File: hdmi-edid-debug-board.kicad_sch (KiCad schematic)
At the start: 87 parts, among them J1 HDMI-A_WE_685119134923, J4 HDMI-A_WE_685119134923, J5 USB-C_GCT_USB4105-GF-A, J6 JST_SH_1x4_SM04B-SRSS-TB-LF-SN, J7 PinHeader_2x3_P2.54mm_Drill1.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, U1 24LC02BT-I/SN, U2 24AA024T-I/SN, U3 NTS0102_TSSOP, U4 TLV70033_SC70, U5 FT4232H_VQFN, U6 TPS2117DRLR, Y1 Oscillator_12MHz_ASFLMB

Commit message: [#77357] Apply post-review changes
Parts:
- removed U1: 24LC02BT-I/SN, antmicro-footprints:SOIC-8_3.9x4.9x1.75mm_P1.27mm, symbol antmicroMemory:24LC02BT-I/SN
- added C8: C_100n_16V_X7R_0402, antmicro-footprints:C_0402_1005Metric, symbol antmicroCapacitors0402:C_100n_16V_X7R_0402
- added D16, D17: TPD2E009_SOT-9X3, antmicro-footprints:SOT-723, symbol antmicroTVSDiodes:TPD2E009_SOT-9X3
- added D18, D19: LED_G_0603_LG_L29K-G2J1-24-Z, antmicro-footprints:LED_0603_1608Metric_G, symbol antmicroLEDIndicationDiscrete:LED_G_0603_LG_L29K-G2J1-24-Z
- added Q1: DMG1012T-7, antmicro-footprints:SOT-523, symbol antmicroTransistorsFETsMOSFETsSingle:DMG1012T-7
- added R13, R14: R_0R_0402, antmicro-footprints:R_0402_1005Metric, symbol antmicroResistors0402:R_0R_0402
- added R25, R27: R_560R_0402, antmicro-footprints:R_0402_1005Metric, symbol antmicroResistors0402:R_560R_0402
- added R26: R_10k_0402, antmicro-footprints:R_0402_1005Metric, symbol antmicroResistors0402:R_10k_0402
- added TP10, TP3, TP4, TP5, TP6, TP7, TP8, TP9: TP_1.5mm_SMD, antmicro-footprints:TP_SMD_1.5mm, symbol antmicroTestPoints:TP_1.5mm_SMD
- U2: now fitted; now in the parts list
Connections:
- net +3V3: now also TP10.1
- net +5V: now also TP9.1
- net EEPROM_5V: now also C8.2, D18.2 (A), TP8.1
- net GND: now also C8.1, D16.3, D17.3, Q1.2 (S), R13.1, R14.1, R25.2, R26.1; no longer U6.4 (PR1), U6.5 (MODE)
- net HDMI_5V: now also D19.2 (A)
- net HDMI_HPD: now also Q1.1 (G), R26.2
- net SINK_SCL: now also D17.2
- net SINK_SDA: now also D17.1
- net SOURCE_SCL: now also D16.2
- net SOURCE_SDA: now also D16.1
- net at U5.12 (ADBUS0): now also TP3.1
- net at U5.13 (ADBUS1): now also TP4.1
- net at U5.14 (ADBUS2): now also TP5.1
- net at U5.15 (ADBUS3): now also TP6.1
- net at U5.25 (BDBUS3): now also TP7.1
- new net: Q1.3 (D), R27.1
- new net: R14.2, U6.4 (PR1)
- new net: D18.1 (C), R25.1
- new net: R13.2, U6.5 (MODE)
- new net: D19.1 (C), R27.2
- no-connect marks 40 -> 35
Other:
- note added: "Alternative MPN: 24LC02BT-I/SN"
- note added: "EDID Selector"
- note added: "HPD indicator"
- note removed: "7bit I2C address 0x50"
- moved on the sheet: C2, C25, C26, C27, C28, C29, C3, C4, C7, D10, D11, D12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

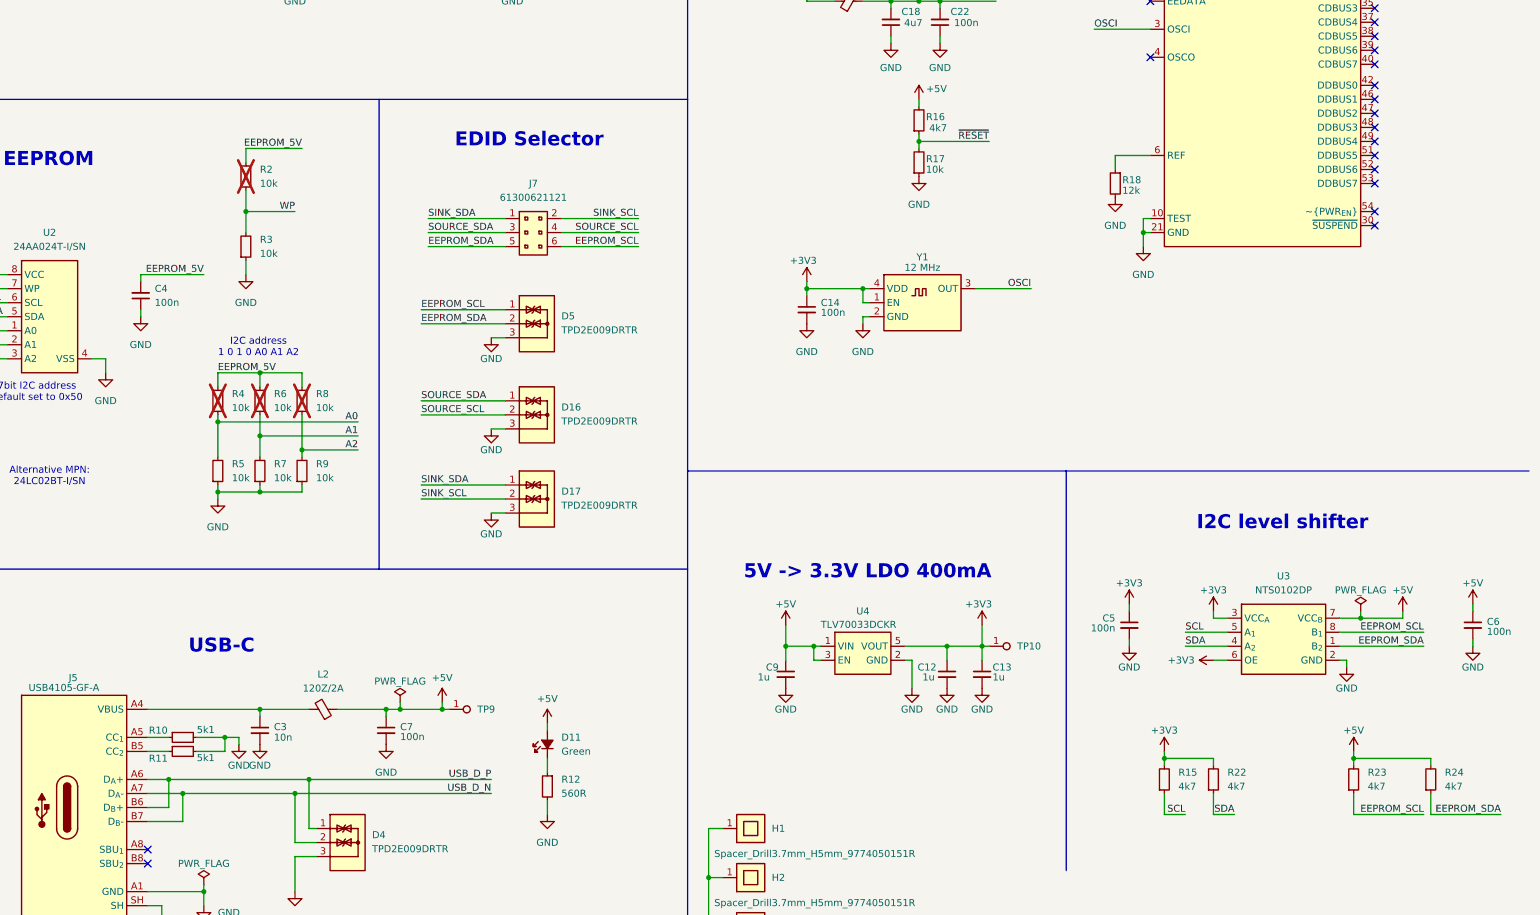
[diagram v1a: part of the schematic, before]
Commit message: [#77357] Add second EDID selector
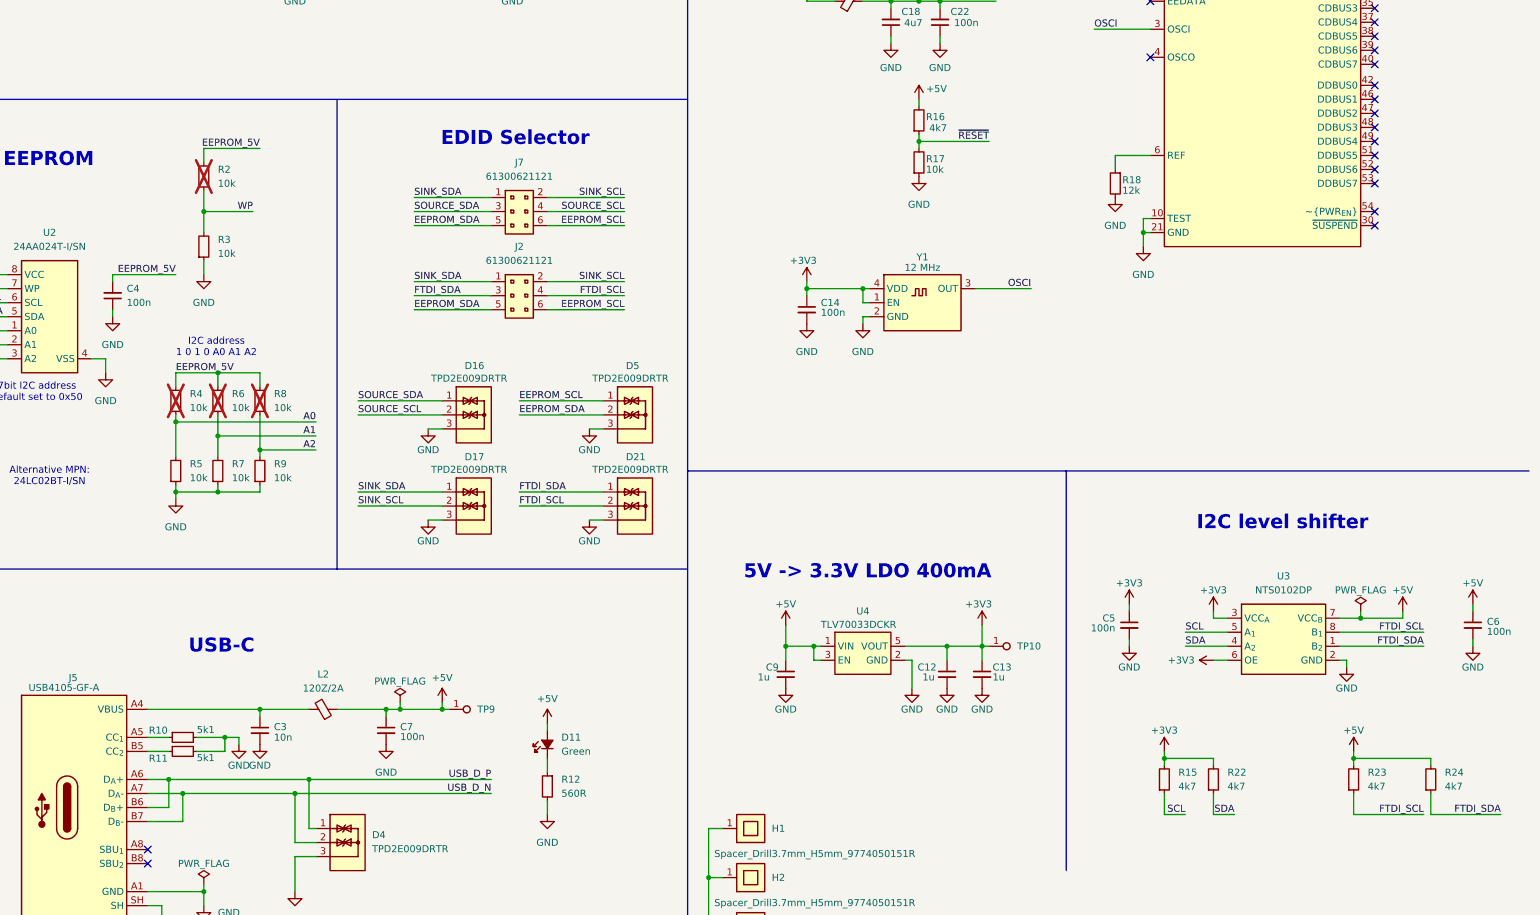
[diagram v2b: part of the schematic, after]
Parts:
- added D21: TPD2E009_SOT-9X3, antmicro-footprints:SOT-723, symbol antmicroTVSDiodes:TPD2E009_SOT-9X3
- added J2: PinHeader_2x3_P2.54mm_Drill1.1mm, antmicro-footprints:PinHeader_2x3_P2.54mm_Drill1.1mm, symbol antmicroGenericPinHeaders:PinHeader_2x3_P2.54mm_Drill1.1mm
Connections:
- net EEPROM_SCL: now also J2.6; no longer R23.1, U3.8 (B_{1})
- net EEPROM_SDA: now also J2.5; no longer R24.1, U3.1 (B_{2})
- net GND: now also D21.3
- net SINK_SCL: now also J2.2
- net SINK_SDA: now also J2.1
- new net FTDI_SCL: D21.2, J2.4, R23.1, U3.8 (B_{1})
- new net FTDI_SDA: D21.1, J2.3, R24.1, U3.1 (B_{2})
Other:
- moved on the sheet: C4, D5, J7, R2, R3, R4, R5, R6, R7, R8, R9

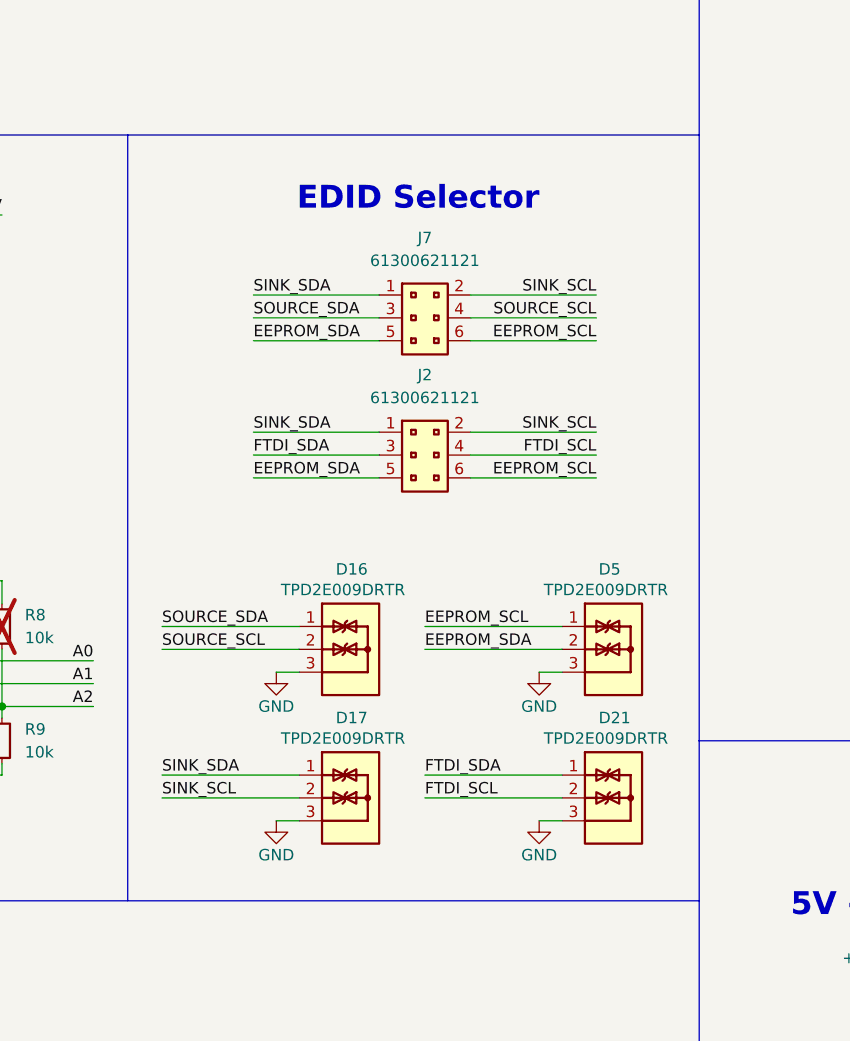
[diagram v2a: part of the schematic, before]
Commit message: [#77357] Align silkscreen, length match HDMI, clean ERC
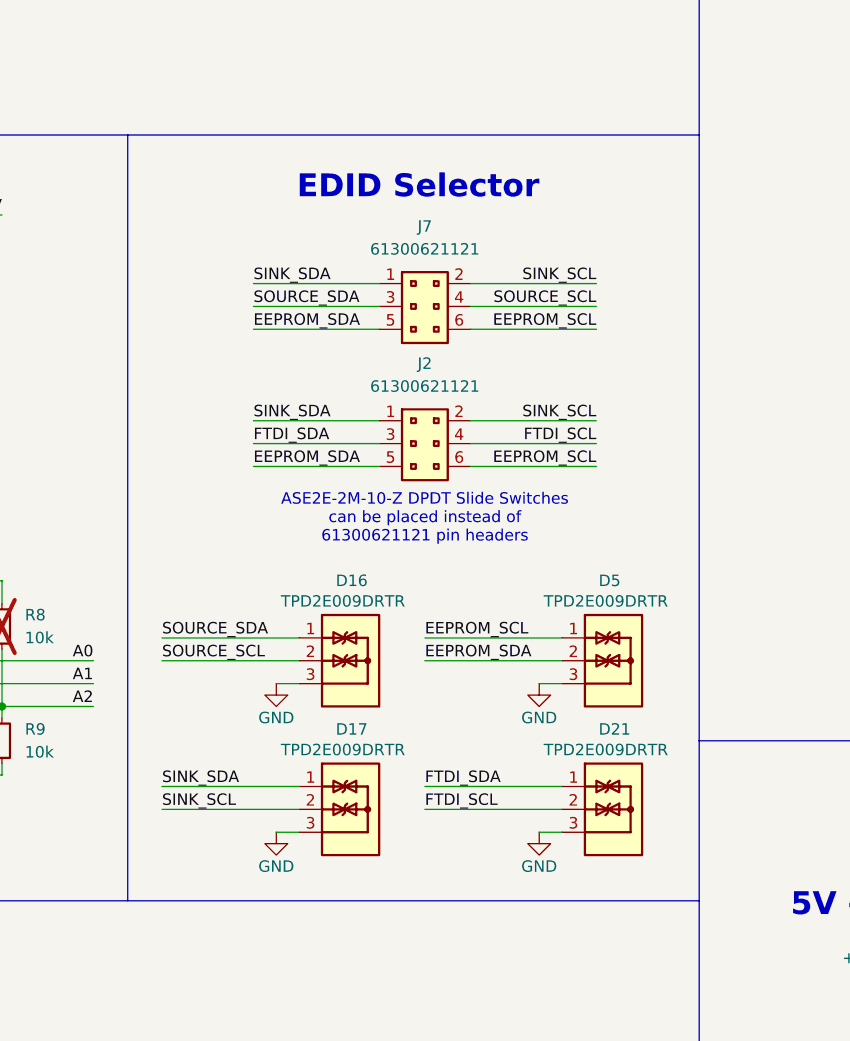
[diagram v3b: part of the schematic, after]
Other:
- note added: "ASE2E-2M-10-Z DPDT Slide Switches can be placed instead of 61300621121 pin headers"
- moved on the sheet: D16, D17, D21, D5, J2, J7

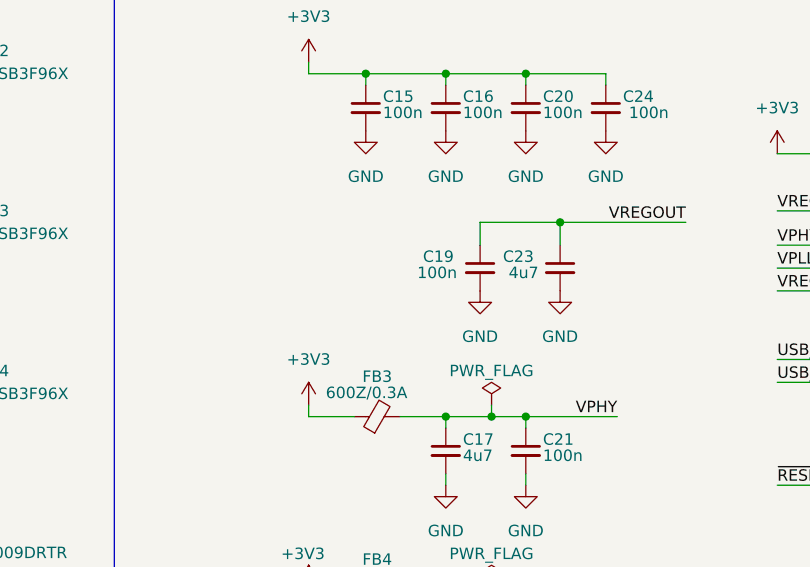
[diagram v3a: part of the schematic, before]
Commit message: [#77357] Add minor fixes
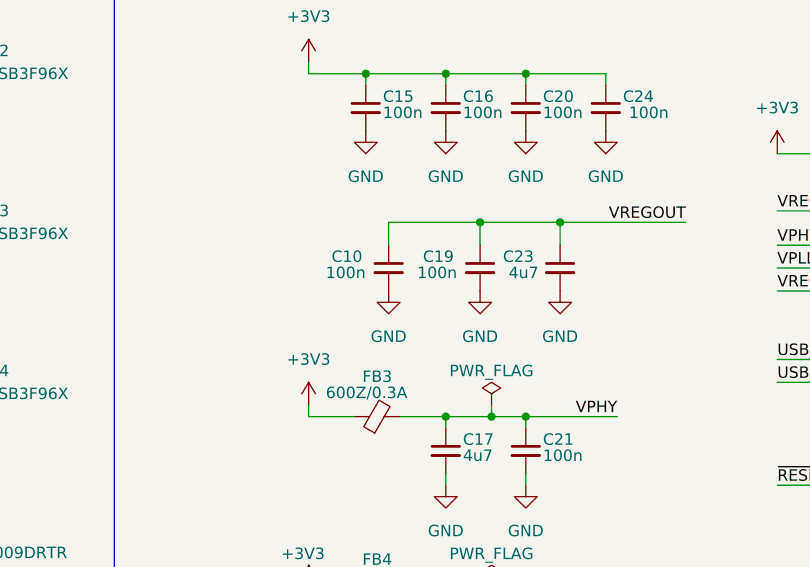
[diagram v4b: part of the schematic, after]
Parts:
- added C10: C_100n_16V_X7R_0402, antmicro-footprints:C_0402_1005Metric, symbol antmicroCapacitors0402:C_100n_16V_X7R_0402
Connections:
- net GND: now also C10.2
- net VREGOUT: now also C10.1

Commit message: [#77357] Synchronize with components library
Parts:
- removed U2: 24AA024T-I/SN, antmicro-footprints:SOIC-8_3.9x4.9x1.75mm_P1.27mm, symbol antmicroMemory:24AA024T-I/SN
- added U2: 24AA024T-I-SN, antmicro-footprints:SOIC-8_3.9x4.9x1.75mm_P1.27mm, symbol antmicroMemory:24AA024T-I-SN
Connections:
- net A0: now also U2.1 (A0)
- net A1: now also U2.2 (A1)
- net A2: now also U2.3 (A2)
- net EEPROM_5V: now also U2.8 (VCC)
- net EEPROM_SCL: now also U2.6 (SCL)
- net EEPROM_SDA: now also U2.5 (SDA)
- net GND: now also U2.4 (VSS)
- net WP: now also U2.7 (WP)
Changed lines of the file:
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@@
 	)
 	(symbol
-		(lib_id "antmicroMemory:24AA024T-I/SN")
-		(at 132.08 144.78 0)
-		(unit 1)
-		(exclude_from_sim no)
-		(in_bom yes)
-		(on_board yes)
-		(dnp no)
-		(fields_autoplaced yes)
-		(property "Reference" "U2"
-			(at 139.7 137.16 0)
-			(effects
-				(font
-					(size 1.27 1.27)
-					(thickness 0.15)
-				)
-			)
-		)
-		(property "Value" "24AA024T-I/SN"
-			(at 160.02 149.86 0)
-			(effects
-				(font
-					(size 1.27 1.27)
-					(thickness 0.15)
-				)
-				(justify left bottom)
-				(hide yes)
-			)
-		)
-		(property "Footprint" "antmicro-footprints:SOIC-8_3.9x4.9x1.75mm_P1.27mm"
-			(at 160.02 152.4 0)
-			(effects
-				(font
-					(size 1.27 1.27)
-					(thickness 0.15)
-				)
-				(justify left bottom)
-				(hide yes)
-			)
-		)
-		(property "Datasheet" "https://www.mouser.com/datasheet/2/268/24AA024_24LC024_24AA025_24LC025_2_Kbit_I2C_Serial_-3005761.pdf"
-			(at 160.02 154.94 0)
-			(effects
-				(font
-					(size 1.27 1.27)
-					(thickness 0.15)
-				)
-				(justify left bottom)
-				(hide yes)
-			)
-		)
-		(property "Description" "EEPROM, 2 Kbit, 256 x 8bit, Serial I2C (2-Wire), 400 kHz, SOIC, 8 Pins"
-			(at 132.08 144.78 0)
-			(effects
-				(font
-					(size 1.27 1.27)
-				)
-				(hide yes)
-			)
-		)
-		(property "MPN" "24AA024T-I/SN"
-			(at 139.7 139.7 0)
-			(effects
-				(font
-					(size 1.27 1.27)
-					(thickness 0.15)
-				)
-			)
-		)
-		(property "Manufacturer" "Microchip Technology"
-			(at 160.02 160.02 0)
-			(effects
-				(font
-					(size 1.27 1.27)
-					(thickness 0.15)
-				)
-				(justify left bottom)
-				(hide yes)
-			)
-		)
-		(property "Author" "Antmicro"
-			(at 160.02 162.56 0)
-			(effects
-				(font
-					(size 1.27 1.27)
-					(thickness 0.15)
-				)
-				(justify left bottom)
-				(hide yes)
-			)
-		)
-		(property "License" "Apache-2.0"
-			(at 160.02 165.1 0)
-			(effects
-				(font
-					(size 1.27 1.27)
-					(thickness 0.15)
-				)
-				(justify left bottom)
-				(hide yes)
-			)
-		)
-		(property "DNP" ""
-			(at 132.08 144.78 0)
-			(effects
-				(font
-					(size 1.27 1.27)
-				)
-				(hide yes)
-			)
-		)
-		(pin "6"
-		)
-		(pin "5"
-		)
-		(pin "3"
-		)
-		(pin "7"
-		)
-		(pin "8"
-		)
-		(pin "2"
-		)
-		(pin "1"
-		)
-		(pin "4"
-		)
-		(instances
-			(project "hdmi-edid-debug-board"
-				(path "/69739539-a836-41d5-a30c-27bc9a8ece0f"
-					(reference "U2")
-					(unit 1)
-				)
-			)
-		)
-	)
-	(symbol
 		(lib_id "antmicroCapacitors0402:C_10n_0402")
 		(at 177.8 224.79 270)
@@
 					(unit 1)
 				)
+			)
+		)
+	)
+	(symbol
+		(lib_id "antmicroMemory:24AA024T-I-SN")
+		(at 132.08 144.78 0)
+		(unit 1)
+		(exclude_from_sim no)
+		(in_bom yes)
+		(on_board yes)
+		(dnp no)
+		(fields_autoplaced yes)
+		(property "Reference" "U2"
+			(at 139.7 137.16 0)
+			(effects
+				(font
+					(size 1.27 1.27)
+					(thickness 0.15)
+				)
+			)
+		)
+		(property "Value" "24AA024T-I-SN"
+			(at 160.02 149.86 0)
+			(effects
+				(font
+					(size 1.27 1.27)
+					(thickness 0.15)
+				)
+				(justify left bottom)
+				(hide yes)
+			)
+		)
+		(property "Footprint" "antmicro-footprints:SOIC-8_3.9x4.9x1.75mm_P1.27mm"
+			(at 160.02 152.4 0)
+			(effects
+				(font
+					(size 1.27 1.27)
+					(thickness 0.15)
+				)
+				(justify left bottom)
+				(hide yes)
+			)
+		)
+		(property "Datasheet" "https://www.mouser.com/datasheet/2/268/24AA024_24LC024_24AA025_24LC025_2_Kbit_I2C_Serial_-3005761.pdf"
+			(at 160.02 154.94 0)
+			(effects
+				(font
+					(size 1.27 1.27)
+					(thickness 0.15)
+				)
+				(justify left bottom)
+				(hide yes)
+			)
+		)
+		(property "Description" "EEPROM, 2 Kbit, 256 x 8bit, Serial I2C (2-Wire), 1.7V-5.5V, 400 kHz, SOIC 8 Pins"
+			(at 160.02 167.005 0)
+			(effects
+				(font
+					(size 1.27 1.27)
+				)
+				(justify left)
+				(hide yes)
+			)
+		)
+		(property "MPN" "24AA024T-I/SN"
+			(at 139.7 139.7 0)
+			(effects
+				(font
+					(size 1.27 1.27)
+					(thickness 0.15)
+				)
+			)
+		)
+		(property "Manufacturer" "Microchip Technology"
+			(at 160.02 160.02 0)
+			(effects
+				(font
+					(size 1.27 1.27)
+					(thickness 0.15)
+				)
+				(justify left bottom)
+				(hide yes)
+			)
+		)
+		(property "Author" "Antmicro"
+			(at 160.02 162.56 0)
+			(effects
+				(font
+					(size 1.27 1.27)
+					(thickness 0.15)
+				)
+				(justify left bottom)
+				(hide yes)
+			)
+		)
+		(property "License" "Apache-2.0"
+			(at 160.02 165.1 0)
+			(effects
+				(font
+					(size 1.27 1.27)
+					(thickness 0.15)
+				)
+				(justify left bottom)
+				(hide yes)
+			)
+		)
+		(pin "8"
+		)
+		(pin "6"
+		)
+		(pin "4"
+		)
+		(pin "7"
+		)
+		(pin "2"
+		)
+		(pin "3"
+		)
+		(pin "5"
+		)
+		(pin "1"
+		)
+		(instances
+			(project ""
+				(path "/69739539-a836-41d5-a30c-27bc9a8ece0f"
+					(reference "U2")
+					(unit 1)
+				)
